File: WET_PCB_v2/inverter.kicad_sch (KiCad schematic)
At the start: 28 parts, among them Q1 IRF530NPBF, Q2 IRF530NPBF, Q3 IRF530NPBF, Q4 IRF530NPBF, U1 IR2110, U2 IR2110

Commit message: notees
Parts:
- removed C8: C, Capacitor_THT:CP_Radial_Tantal_D5.0mm_P5.00mm, symbol Device:C_Polarized
- added C8: B32529C1104K000, Capacitor_THT:C_Rect_L7.0mm_W2.5mm_P5.00mm, symbol B32529C1104K000:B32529C1104K000
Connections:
- net Vout_Inverter_+: now also C8.1
- net Vout_Inverter_-: now also C8.2
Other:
- note added: "add second cap"
- note removed: "different cap?"
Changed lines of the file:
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@@
 	(generator_version "10.0")
 	(paper "A4")
-	(text "different cap?\n"
+	(text "add second cap"
 		(exclude_from_sim no)
-		(at 147.574 72.136 0)
+		(at 36.322 44.958 0)
+		(effects
+			(font
+				(size 1.27 1.27)
+			)
+		)
+	)
+	(text "add second cap"
+		(exclude_from_sim no)
+		(at 261.366 47.752 0)
 		(effects
 			(font
@@
 	)
 	(junction
+		(at 153.67 67.31)
+		(diameter 0)
+		(color 0 0 0 0)
+	)
+	(junction
 		(at 147.32 25.4)
 		(diameter 0)
@@
 	)
 	(junction
+		(at 140.97 66.04)
+		(diameter 0)
+		(color 0 0 0 0)
+	)
+	(junction
 		(at 64.77 49.53)
 		(diameter 0)
@@
 	)
 	(junction
+		(at 153.67 66.04)
+		(diameter 0)
+		(color 0 0 0 0)
+	)
+	(junction
 		(at 153.67 53.34)
 		(diameter 0)
@@
 	)
 	(junction
-		(at 153.67 63.5)
-		(diameter 0)
-		(color 0 0 0 0)
-	)
-	(junction
 		(at 217.17 71.12)
 		(diameter 0)
@@
 	)
 	(junction
-		(at 140.97 63.5)
+		(at 140.97 67.31)
 		(diameter 0)
 		(color 0 0 0 0)
@@
 	(wire
 		(pts
-			(xy 153.67 63.5) (xy 153.67 87.63)
-		)
-		(stroke
-			(width 0)
-			(type default)
-		)
-	)
-	(wire
-		(pts
 			(xy 210.82 77.47) (xy 217.17 77.47)
 		)
@@
 	(wire
 		(pts
-			(xy 153.67 53.34) (xy 153.67 63.5)
+			(xy 153.67 53.34) (xy 153.67 66.04)
 		)
 		(stroke
@@
 	(wire
 		(pts
-			(xy 140.97 63.5) (xy 143.51 63.5)
+			(xy 140.97 66.04) (xy 143.51 66.04)
 		)
 		(stroke
@@
 	(wire
 		(pts
+			(xy 140.97 67.31) (xy 140.97 87.63)
+		)
+		(stroke
+			(width 0)
+			(type default)
+		)
+	)
+	(wire
+		(pts
 			(xy 217.17 64.77) (xy 215.9 64.77)
 		)
@@
 	(wire
 		(pts
-			(xy 91.44 46.99) (xy 97.79 46.99)
+			(xy 153.67 66.04) (xy 153.67 67.31)
 		)
 		(stroke
@@
 	(wire
 		(pts
-			(xy 29.21 19.05) (xy 26.67 19.05)
+			(xy 91.44 46.99) (xy 97.79 46.99)
 		)
 		(stroke
@@
 	(wire
 		(pts
-			(xy 97.79 64.77) (xy 106.68 64.77)
+			(xy 29.21 19.05) (xy 26.67 19.05)
 		)
 		(stroke
@@
 	(wire
 		(pts
-			(xy 44.45 72.39) (xy 44.45 74.93)
+			(xy 97.79 64.77) (xy 106.68 64.77)
 		)
 		(stroke
@@
 	(wire
 		(pts
-			(xy 147.32 25.4) (xy 166.37 25.4)
+			(xy 44.45 72.39) (xy 44.45 74.93)
 		)
 		(stroke
@@
 	(wire
 		(pts
-			(xy 196.85 64.77) (xy 196.85 77.47)
+			(xy 147.32 25.4) (xy 166.37 25.4)
 		)
 		(stroke
@@
 	(wire
 		(pts
-			(xy 140.97 53.34) (xy 140.97 63.5)
+			(xy 196.85 64.77) (xy 196.85 77.47)
 		)
 		(stroke
@@
 	(wire
 		(pts
+			(xy 153.67 67.31) (xy 153.67 87.63)
+		)
+		(stroke
+			(width 0)
+			(type default)
+		)
+	)
+	(wire
+		(pts
 			(xy 196.85 64.77) (xy 187.96 64.77)
 		)
@@
 	(wire
 		(pts
-			(xy 151.13 63.5) (xy 153.67 63.5)
+			(xy 151.13 66.04) (xy 153.67 66.04)
 		)
 		(stroke
@@
 	(wire
 		(pts
+			(xy 140.97 66.04) (xy 140.97 67.31)
+		)
+		(stroke
+			(width 0)
+			(type default)
+		)
+	)
+	(wire
+		(pts
 			(xy 58.42 39.37) (xy 77.47 39.37)
 		)
@@
 	(wire
 		(pts
-			(xy 140.97 63.5) (xy 140.97 87.63)
+			(xy 140.97 53.34) (xy 140.97 66.04)
 		)
 		(stroke
@@
 	)
 	(symbol
-		(lib_id "Device:C_Polarized")
-		(at 147.32 63.5 90)
+		(lib_id "B32529C1104K000:B32529C1104K000")
+		(at 140.97 67.31 0)
 		(unit 1)
 		(body_style 1)
@@
 		(fields_autoplaced yes)
 		(property "Reference" "C8"
-			(at 146.431 55.88 90)
+			(at 147.32 59.69 0)
 			(show_name no)
 			(do_not_autoplace no)
@@
 			)
 		)
-		(property "Value" "C"
-			(at 146.431 58.42 90)
+		(property "Value" "B32529C1104K000"
+			(at 147.32 62.23 0)
 			(show_name no)
 			(do_not_autoplace no)
@@
 			)
 		)
-		(property "Footprint" "Capacitor_THT:CP_Radial_Tantal_D5.0mm_P5.00mm"
-			(at 151.13 62.5348 0)
+		(property "Footprint" "Capacitor_THT:C_Rect_L7.0mm_W2.5mm_P5.00mm"
+			(at 149.86 163.5 0)
 			(hide yes)
 			(show_name no)
@@
 					(size 1.27 1.27)
 				)
+				(justify left top)
 			)
 		)
-		(property "Datasheet" ""
-			(at 147.32 63.5 0)
+		(property "Datasheet" "https://product.tdk.com/system/files/dam/doc/product/capacitor/film/mkt/data_sheet/20/20/db/fc_2009/b32520_529.pdf"
+			(at 149.86 263.5 0)
 			(hide yes)
 			(show_name no)
@@
 					(size 1.27 1.27)
 				)
+				(justify left top)
 			)
 		)
-		(property "Description" "Polarized capacitor"
-			(at 147.32 63.5 0)
+		(property "Description" "EPCOS - B32529C1104K000 - General Purpose Film Capacitor, Metallized PET Stacked, Radial Box - 2 Pin, 0.1 F, +/- 10%, 63 V//"
+			(at 140.97 67.31 0)
 			(hide yes)
 			(show_name no)
@@
 			)
 		)
-		(pin "2"
+		(property "Height" "6.5"
+			(at 149.86 463.5 0)
+			(hide yes)
+			(show_name no)
+			(do_not_autoplace no)
+			(effects
+				(font
+					(size 1.27 1.27)
+				)
+				(justify left top)
+			)
+		)
+		(property "Farnell Part Number" ""
+			(at 149.86 563.5 0)
+			(hide yes)
+			(show_name no)
+			(do_not_autoplace no)
+			(effects
+				(font
+					(size 1.27 1.27)
+				)
+				(justify left top)
+			)
+		)
+		(property "Farnell Price/Stock" ""
+			(at 149.86 663.5 0)
+			(hide yes)
+			(show_name no)
+			(do_not_autoplace no)
+			(effects
+				(font
+					(size 1.27 1.27)
+				)
+				(justify left top)
+			)
+		)
+		(property "Manufacturer_Name" "TDK"
+			(at 149.86 763.5 0)
+			(hide yes)
+			(show_name no)
+			(do_not_autoplace no)
+			(effects
+				(font
+					(size 1.27 1.27)
+				)
+				(justify left top)
+			)
+		)
+		(property "Manufacturer_Part_Number" "B32529C1104K000"
+			(at 149.86 863.5 0)
+			(hide yes)
+			(show_name no)
+			(do_not_autoplace no)
+			(effects
+				(font
+					(size 1.27 1.27)
+				)
+				(justify left top)
+			)
 		)
 		(pin "1"
 		)
+		(pin "2"
+		)
 		(instances

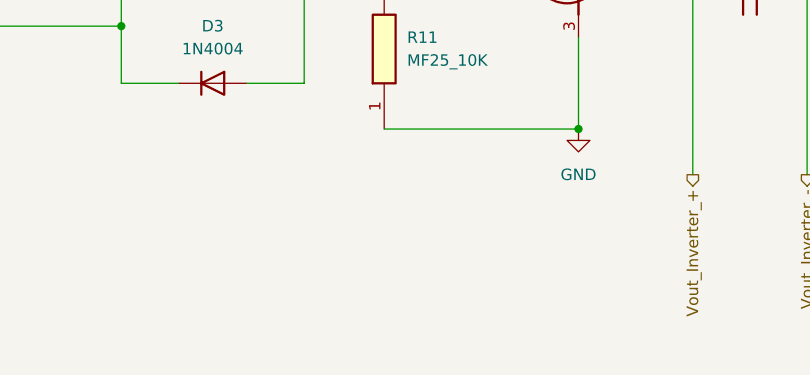
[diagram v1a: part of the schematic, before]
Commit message: redid part of layout inverter
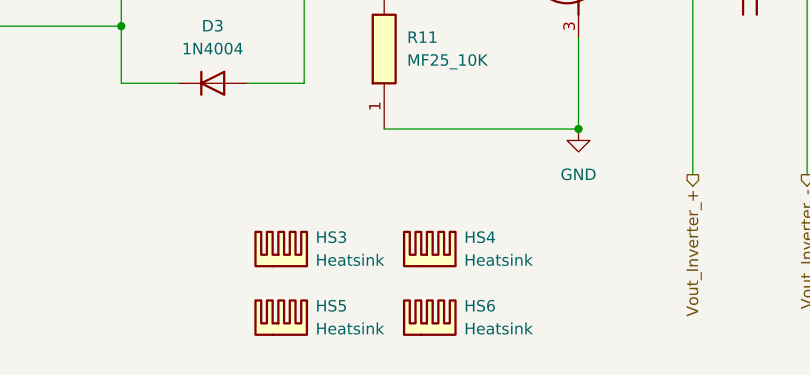
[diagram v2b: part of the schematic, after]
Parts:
- added HS3, HS4, HS5, HS6: Heatsink, Heatsink:Heatsink_AAVID_Extruded_531002B02100G_34.9x12.7mm_H25.4mm, symbol Mechanical:Heatsink

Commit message: before i prob fuck up everything bc clearance
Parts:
- removed C3: B32529C1104K000, Capacitor_THT:C_Rect_L7.0mm_W2.5mm_P5.00mm, symbol B32529C1104K000:B32529C1104K000
- added C25, C26: C322C104K5R5TA, Capacitor_THT:C_Disc_D4.3mm_W1.9mm_P5.00mm, symbol C322C104K5R5TA:C322C104K5R5TA
- added C3: C, symbol Device:C
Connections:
- net GND: now also C25.1, C26.2
- net VDD_Driver_Inverter: now also C25.2, C26.1
- net Vout_Inverter_+: now also C3.1
- net Vout_Inverter_-: now also C3.2

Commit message: im gonna start to route and probably revert to this version at least 5 times
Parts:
- C3: footprint (none) -> Capacitor_THT:C_Rect_L32.0mm_W15.0mm_P27.00mm
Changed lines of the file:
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@@
 			)
 		)
-		(property "Footprint" ""
+		(property "Footprint" "Capacitor_THT:C_Rect_L32.0mm_W15.0mm_P27.00mm"
 			(at 151.13 52.3748 0)
 			(hide yes)

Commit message: veel routes weinig goeds
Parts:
- added C17: C, Inductor_THT:L_Axial_L23.4mm_D12.7mm_P32.00mm_Horizontal_Vishay_IHA-203, symbol Device:C
- added C20: C, Capacitor_THT:C_Rect_L24.0mm_W12.8mm_P22.50mm_MKT, symbol Device:C
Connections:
- net Vout_Inverter_+: now also C17.1, C20.1
- net Vout_Inverter_-: now also C17.2, C20.2
